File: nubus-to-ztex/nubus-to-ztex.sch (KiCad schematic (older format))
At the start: 0 parts

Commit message: forgot to commit last attempt at V1.2
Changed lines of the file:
@@
 $Descr A4 11693 8268
 encoding utf-8
-Sheet 1 7
+Sheet 1 9
 Title ""
 Date ""
@@
 F1 "vga.sch" 50
 $EndSheet
+$Sheet
+S 1000 3300 1000 550
+U 62D70B59
+F0 "sdcard" 50
+F1 "sdcard.sch" 50
+$EndSheet
+$Sheet
+S 2250 3300 1000 550
+U 62CC4C0A
+F0 "pmod" 50
+F1 "pmod.sch" 50
+$EndSheet
 $EndSCHEMATC

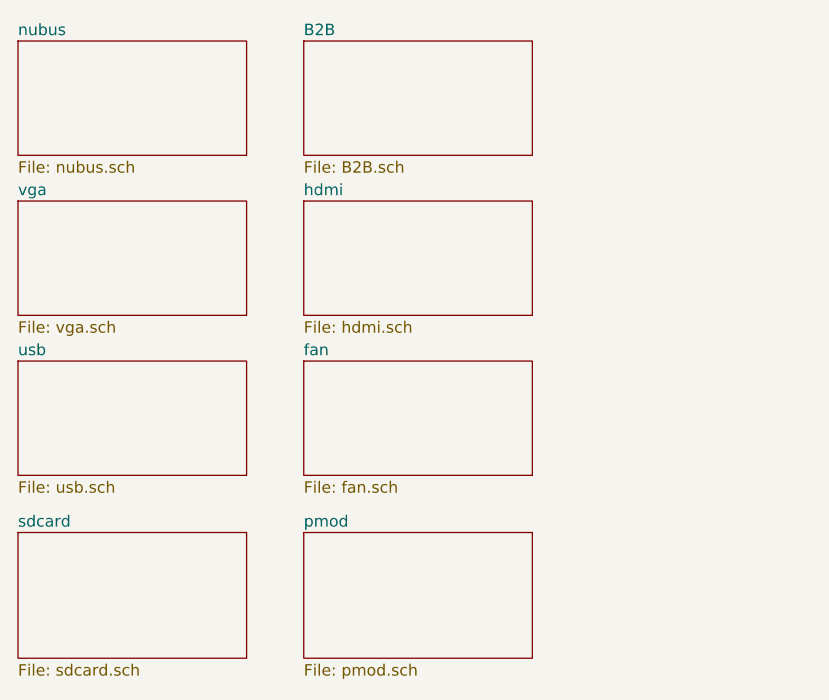
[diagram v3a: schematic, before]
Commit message: move shielding to hdmi, trace cleanup
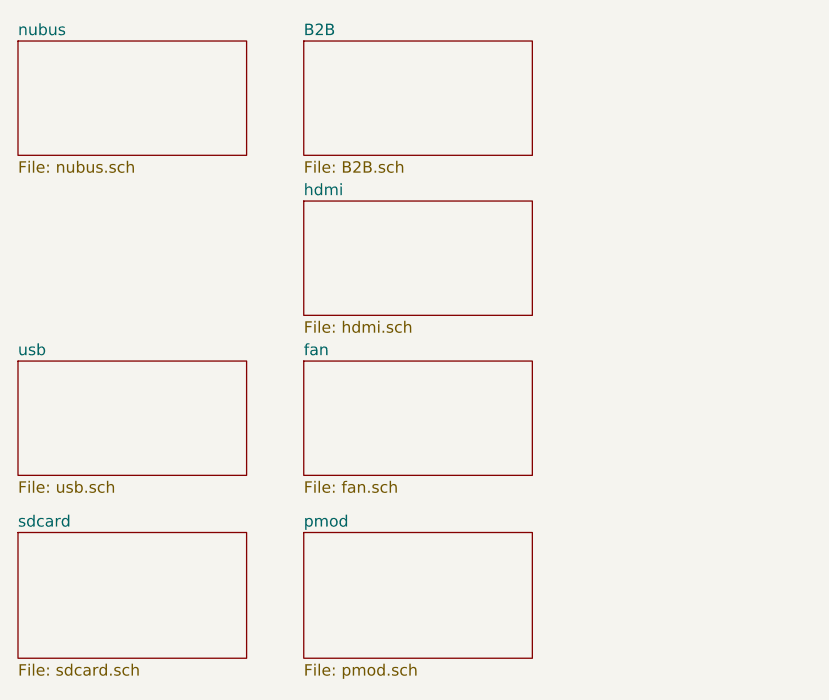
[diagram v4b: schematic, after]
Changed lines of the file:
@@
 $Descr A4 11693 8268
 encoding utf-8
-Sheet 1 9
+Sheet 1 8
 Title ""
 Date ""
@@
 $EndSheet
 $Sheet
-S 1000 1850 1000 500
-U 6193AB43
-F0 "vga" 50
-F1 "vga.sch" 50
-$EndSheet
-$Sheet

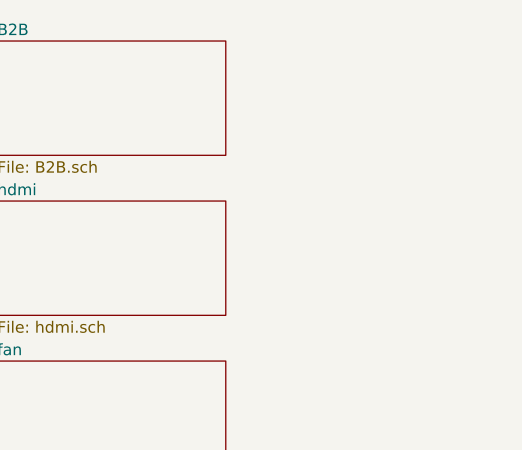
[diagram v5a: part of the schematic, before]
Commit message: more update to V1.2 to try to limit cost
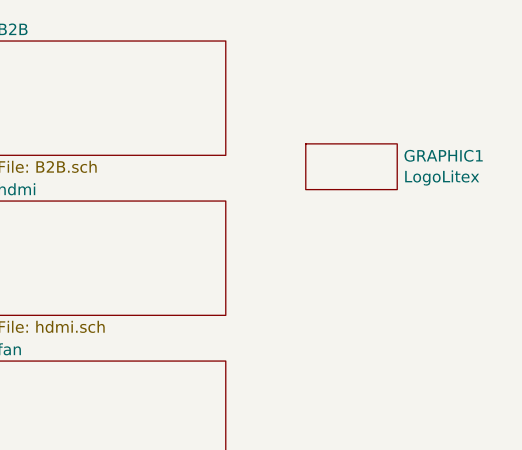
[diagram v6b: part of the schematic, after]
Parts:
- added GRAPHIC1: LogoLitex, For_SeeedStudio:litex_logo, symbol logo:LogoLitex
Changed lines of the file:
@@
 F1 "pmod.sch" 50
 $EndSheet
+$Comp
+L logo:LogoLitex GRAPHIC1
+U 1 1 637CDFF9
+P 3800 1650
+F 0 "GRAPHIC1" H 4028 1646 50  0000 L CNN
+F 1 "LogoLitex" H 4028 1555 50  0000 L CNN
+F 2 "For_SeeedStudio:litex_logo" H 3800 1650 50  0001 C CNN
+F 3 "" H 3800 1650 50  0001 C CNN
+	1    3800 1650
+	1    0    0    -1
+$EndComp
 $EndSCHEMATC

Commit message: BoM, power plane, serial back to THT, ...
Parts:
- GRAPHIC1: DNP (none) -> DNP
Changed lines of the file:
@@
 F 2 "For_SeeedStudio:litex_logo" H 3800 1650 50  0001 C CNN
 F 3 "" H 3800 1650 50  0001 C CNN
+F 4 "DNP" H 3800 1650 50  0001 C CNN "DNP"
 	1    3800 1650
 	1    0    0    -1

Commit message: update
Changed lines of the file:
@@
 $Descr A4 11693 8268
 encoding utf-8
-Sheet 1 8
+Sheet 1 9
 Title ""
 Date ""
@@
 	1    0    0    -1
 $EndComp
+$Sheet
+S 1000 1850 1000 500
+U 64F8CFB4
+F0 "clock" 50
+F1 "clock.sch" 50
+$EndSheet
 $EndSCHEMATC
